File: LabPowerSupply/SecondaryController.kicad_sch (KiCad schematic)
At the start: 15 parts

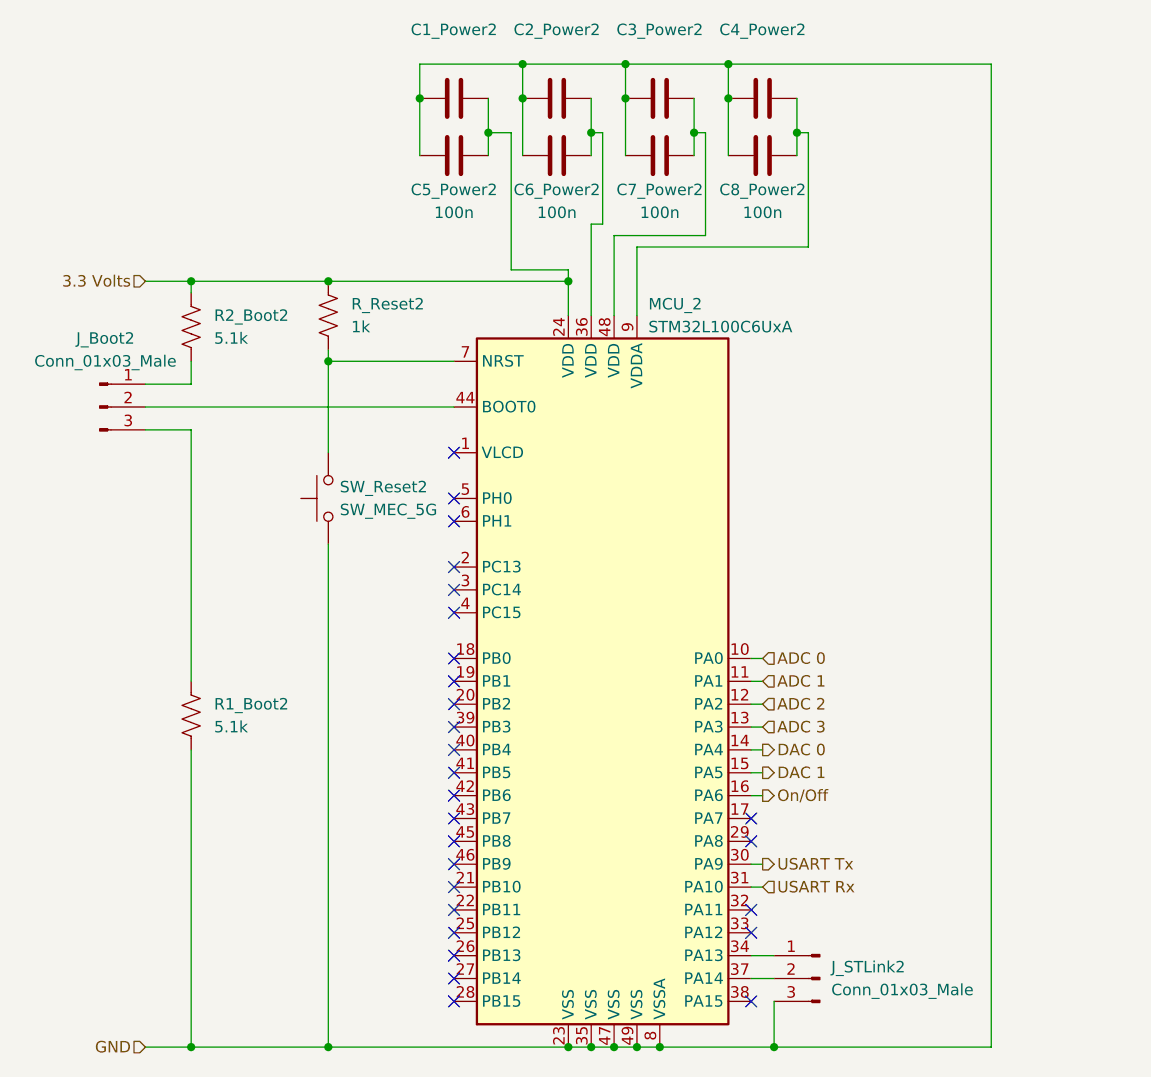
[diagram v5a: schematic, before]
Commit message: Added oscillator to mcu2
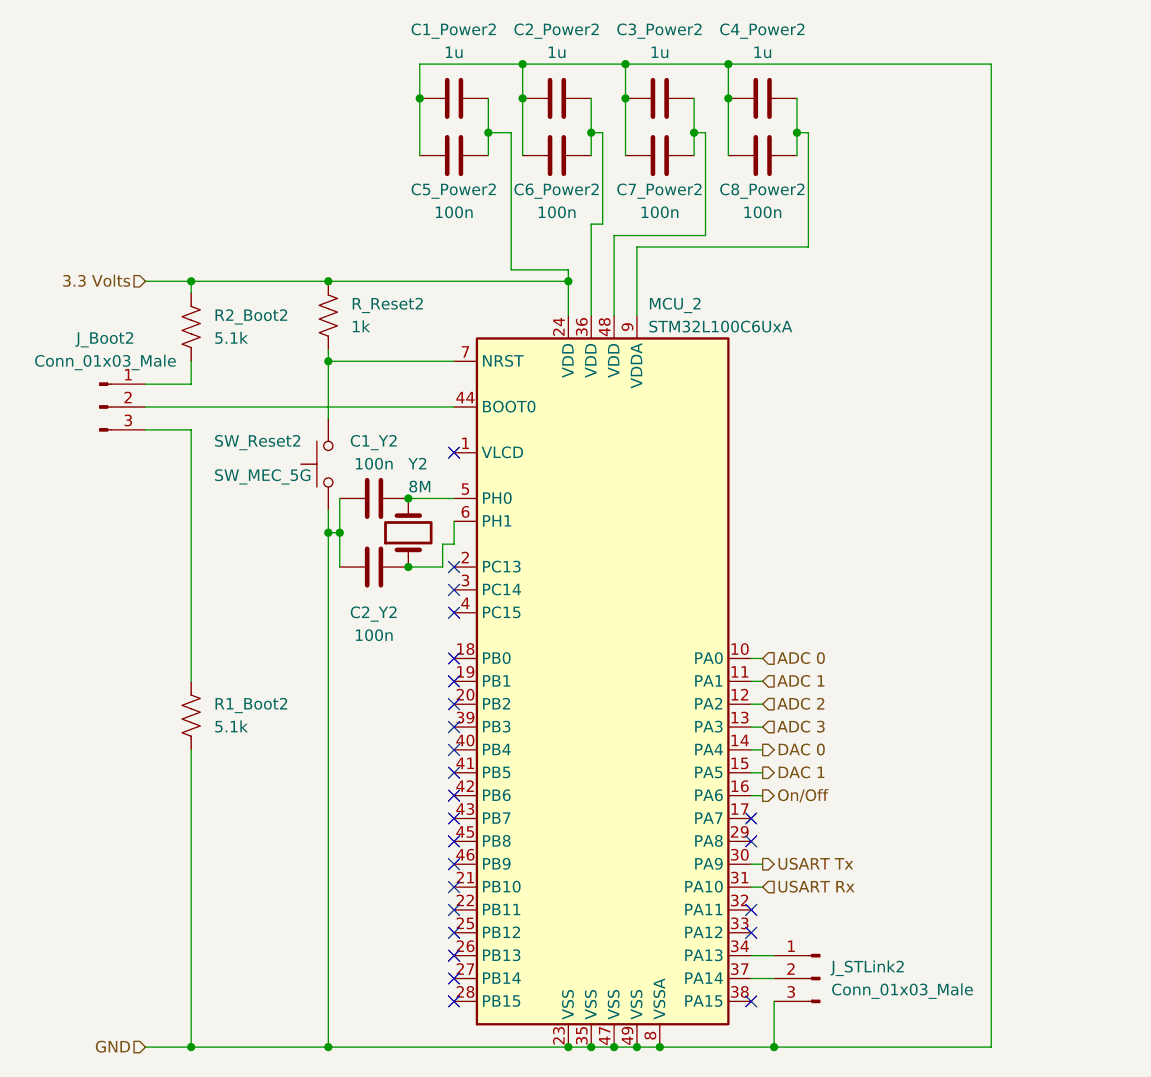
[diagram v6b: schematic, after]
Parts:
- added C1_Y2, C2_Y2: 100n, Capacitor_THT:C_Disc_D5.0mm_W2.5mm_P2.50mm, symbol Device:C
- added Y2: 8M, Crystal:Crystal_HC18-U_Vertical, symbol Device:Crystal
- C1_Power2, C2_Power2, C3_Power2, C4_Power2: value (none) -> 1u
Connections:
- net GND: now also C1_Y2.1, C2_Y2.1
- net at MCU_2.5 (PH0): now also C1_Y2.2, Y2.2
- net at MCU_2.6 (PH1): now also C2_Y2.2, Y2.1
- no-connect marks 27 -> 25
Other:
- moved on the sheet: SW_Reset2
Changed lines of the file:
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@@
   (junction (at 68.58 139.7) (diameter 0) (color 0 0 0 0)
   )
+  (junction (at 68.58 82.55) (diameter 0) (color 0 0 0 0)
+  )
   (junction (at 118.11 139.7) (diameter 0) (color 0 0 0 0)
   )
@@
   (junction (at 95.25 54.61) (diameter 0) (color 0 0 0 0)
   )
+  (junction (at 69.85 82.55) (diameter 0) (color 0 0 0 0)
+  )
+  (junction (at 77.47 86.36) (diameter 0) (color 0 0 0 0)
+  )
   (junction (at 90.17 34.29) (diameter 0) (color 0 0 0 0)
   )
@@
   )
   (junction (at 86.36 38.1) (diameter 0) (color 0 0 0 0)
+  )
+  (junction (at 77.47 78.74) (diameter 0) (color 0 0 0 0)
   )
   (junction (at 105.41 139.7) (diameter 0) (color 0 0 0 0)
@@
   (no_connect (at 82.55 88.9))
   (no_connect (at 82.55 91.44))
-  (no_connect (at 82.55 81.28))
   (no_connect (at 82.55 73.66))
-  (no_connect (at 82.55 78.74))
   (no_connect (at 82.55 96.52))
   (wire (pts (xy 90.17 34.29) (xy 90.17 40.64))
@@
     (stroke (width 0) (type default) (color 0 0 0 0))
   )
+  (wire (pts (xy 82.55 83.82) (xy 81.28 83.82))
+    (stroke (width 0) (type default) (color 0 0 0 0))
+  )
   (wire (pts (xy 88.9 53.34) (xy 95.25 53.34))
     (stroke (width 0) (type default) (color 0 0 0 0))
@@
     (stroke (width 0) (type default) (color 0 0 0 0))
   )
+  (wire (pts (xy 68.58 82.55) (xy 69.85 82.55))
+    (stroke (width 0) (type default) (color 0 0 0 0))
+  )
   (wire (pts (xy 95.25 53.34) (xy 95.25 54.61))
     (stroke (width 0) (type default) (color 0 0 0 0))
@@
     (stroke (width 0) (type default) (color 0 0 0 0))
   )
+  (wire (pts (xy 68.58 82.55) (xy 68.58 139.7))
+    (stroke (width 0) (type default) (color 0 0 0 0))
+  )
   (wire (pts (xy 86.36 34.29) (xy 86.36 38.1))
     (stroke (width 0) (type default) (color 0 0 0 0))
@@
     (stroke (width 0) (type default) (color 0 0 0 0))
   )
+  (wire (pts (xy 69.85 78.74) (xy 69.85 82.55))
+    (stroke (width 0) (type default) (color 0 0 0 0))
+  )
+  (wire (pts (xy 81.28 83.82) (xy 81.28 86.36))
+    (stroke (width 0) (type default) (color 0 0 0 0))
+  )
   (wire (pts (xy 142.24 139.7) (xy 118.11 139.7))
     (stroke (width 0) (type default) (color 0 0 0 0))
@@
     (stroke (width 0) (type default) (color 0 0 0 0))
   )
+  (wire (pts (xy 77.47 78.74) (xy 82.55 78.74))
+    (stroke (width 0) (type default) (color 0 0 0 0))
+  )
   (wire (pts (xy 97.79 38.1) (xy 97.79 40.64))
     (stroke (width 0) (type default) (color 0 0 0 0))
@@
     (stroke (width 0) (type default) (color 0 0 0 0))
   )
+  (wire (pts (xy 82.55 83.82) (xy 82.55 81.28))
+    (stroke (width 0) (type default) (color 0 0 0 0))
+  )
   (wire (pts (xy 68.58 54.61) (xy 95.25 54.61))
     (stroke (width 0) (type default) (color 0 0 0 0))
@@
     (stroke (width 0) (type default) (color 0 0 0 0))
   )
+  (wire (pts (xy 81.28 86.36) (xy 77.47 86.36))
+    (stroke (width 0) (type default) (color 0 0 0 0))
+  )
   (wire (pts (xy 142.24 30.48) (xy 113.03 30.48))
     (stroke (width 0) (type default) (color 0 0 0 0))
@@
     (stroke (width 0) (type default) (color 0 0 0 0))
   )
-  (wire (pts (xy 68.58 83.82) (xy 68.58 139.7))
+  (wire (pts (xy 69.85 82.55) (xy 69.85 86.36))
+    (stroke (width 0) (type default) (color 0 0 0 0))
+  )
+  (wire (pts (xy 68.58 80.01) (xy 68.58 82.55))
     (stroke (width 0) (type default) (color 0 0 0 0))
   )
@@
     (stroke (width 0) (type default) (color 0 0 0 0))
   )
-  (wire (pts (xy 68.58 63.5) (xy 68.58 73.66))
+  (wire (pts (xy 68.58 63.5) (xy 68.58 69.85))
     (stroke (width 0) (type default) (color 0 0 0 0))
   )
@@
     )
     (property "Datasheet" "~" (id 3) (at 116.84 40.64 0)
+      (effects (font (size 1.27 1.27)) hide)
+    )
+    (pin "1")
+    (pin "2")
+  )
+  (symbol (lib_id "Device:C") (at 73.66 86.36 90) (mirror x) (unit 1)
+    (in_bom yes) (on_board yes)
+    (property "Reference" "C2_Y2" (id 0) (at 73.66 91.44 90))
+    (property "Value" "100n" (id 1) (at 73.66 93.98 90))
+    (property "Footprint" "Capacitor_THT:C_Disc_D5.0mm_W2.5mm_P2.50mm" (id 2) (at 77.47 87.3252 0)
+      (effects (font (size 1.27 1.27)) hide)
+    )
+    (property "Datasheet" "~" (id 3) (at 73.66 86.36 0)
       (effects (font (size 1.27 1.27)) hide)
     )
@@
     (in_bom yes) (on_board yes) (fields_autoplaced)
     (property "Reference" "C1_Power2" (id 0) (at 82.55 26.67 90))
-    (property "Value" "" (id 1) (at 82.55 29.21 90))
+    (property "Value" "1u" (id 1) (at 82.55 29.21 90))
     (property "Footprint" "Capacitor_THT:C_Disc_D5.0mm_W2.5mm_P2.50mm" (id 2) (at 86.36 33.3248 0)
       (effects (font (size 1.27 1.27)) hide)
@@
     (in_bom yes) (on_board yes) (fields_autoplaced)
     (property "Reference" "C2_Power2" (id 0) (at 93.98 26.67 90))
-    (property "Value" "" (id 1) (at 93.98 29.21 90))
+    (property "Value" "1u" (id 1) (at 93.98 29.21 90))
     (property "Footprint" "Capacitor_THT:C_Disc_D5.0mm_W2.5mm_P2.50mm" (id 2) (at 97.79 33.3248 0)
       (effects (font (size 1.27 1.27)) hide)
@@
     (pin "2")
   )
+  (symbol (lib_id "Device:C") (at 73.66 78.74 90) (unit 1)
+    (in_bom yes) (on_board yes)
+    (property "Reference" "C1_Y2" (id 0) (at 73.66 72.39 90))
+    (property "Value" "100n" (id 1) (at 73.66 74.93 90))
+    (property "Footprint" "Capacitor_THT:C_Disc_D5.0mm_W2.5mm_P2.50mm" (id 2) (at 77.47 77.7748 0)
+      (effects (font (size 1.27 1.27)) hide)
+    )
+    (property "Datasheet" "~" (id 3) (at 73.66 78.74 0)
+      (effects (font (size 1.27 1.27)) hide)
+    )
+    (pin "1")
+    (pin "2")
+  )
   (symbol (lib_id "Device:C") (at 105.41 34.29 90) (unit 1)
     (in_bom yes) (on_board yes) (fields_autoplaced)
     (property "Reference" "C3_Power2" (id 0) (at 105.41 26.67 90))
-    (property "Value" "" (id 1) (at 105.41 29.21 90))
+    (property "Value" "1u" (id 1) (at 105.41 29.21 90))
     (property "Footprint" "Capacitor_THT:C_Disc_D5.0mm_W2.5mm_P2.50mm" (id 2) (at 109.22 33.3248 0)
       (effects (font (size 1.27 1.27)) hide)
@@
     (pin "2")
   )
+  (symbol (lib_id "Device:Crystal") (at 77.47 82.55 90) (unit 1)
+    (in_bom yes) (on_board yes)
+    (property "Reference" "Y2" (id 0) (at 77.47 74.93 90)
+      (effects (font (size 1.27 1.27)) (justify right))
+    )
+    (property "Value" "8M" (id 1) (at 77.47 77.47 90)
+      (effects (font (size 1.27 1.27)) (justify right))
+    )
+    (property "Footprint" "Crystal:Crystal_HC18-U_Vertical" (id 2) (at 77.47 82.55 0)
+      (effects (font (size 1.27 1.27)) hide)
+    )
+    (property "Datasheet" "~" (id 3) (at 77.47 82.55 0)
+      (effects (font (size 1.27 1.27)) hide)
+    )
+    (pin "1")
+    (pin "2")
+  )
   (symbol (lib_id "Device:C") (at 116.84 34.29 90) (unit 1)
     (in_bom yes) (on_board yes) (fields_autoplaced)
     (property "Reference" "C4_Power2" (id 0) (at 116.84 26.67 90))
-    (property "Value" "" (id 1) (at 116.84 29.21 90))
+    (property "Value" "1u" (id 1) (at 116.84 29.21 90))
     (property "Footprint" "Capacitor_THT:C_Disc_D5.0mm_W2.5mm_P2.50mm" (id 2) (at 120.65 33.3248 0)
       (effects (font (size 1.27 1.27)) hide)
@@
     (pin "2")
   )
-  (symbol (lib_id "Switch:SW_MEC_5G") (at 68.58 78.74 90) (unit 1)
-    (in_bom yes) (on_board yes) (fields_autoplaced)
-    (property "Reference" "SW_Reset2" (id 0) (at 69.85 77.4699 90)
+  (symbol (lib_id "Switch:SW_MEC_5G") (at 68.58 74.93 90) (unit 1)
+    (in_bom yes) (on_board yes)
+    (property "Reference" "SW_Reset2" (id 0) (at 55.88 72.39 90)
       (effects (font (size 1.27 1.27)) (justify right))
     )
-    (property "Value" "SW_MEC_5G" (id 1) (at 69.85 80.0099 90)
+    (property "Value" "SW_MEC_5G" (id 1) (at 55.88 76.2 90)
       (effects (font (size 1.27 1.27)) (justify right))
     )
-    (property "Footprint" "Button_Switch_SMD:SW_MEC_5GSH9" (id 2) (at 63.5 78.74 0)
-      (effects (font (size 1.27 1.27)) hide)
-    )
-    (property "Datasheet" "http://www.apem.com/int/index.php?controller=attachment&id_attachment=488" (id 3) (at 63.5 78.74 0)
-      (effects (font (size 1.27 1.27)) hide)
-    )
+    (property "Footprint" "Button_Switch_SMD:SW_MEC_5GSH9" (id 2) (at 63.5 74.93 0)
+      (effects (font (size 1.27 1.27)) hide)
+    )
+    (property "Datasheet" "http://www.apem.com/int/index.php?controller=attachment&id_attachment=488" (id 3) (at 63.5 74.93 0)
+      (effects (font (size 1.27 1.27)) hide)
+    )

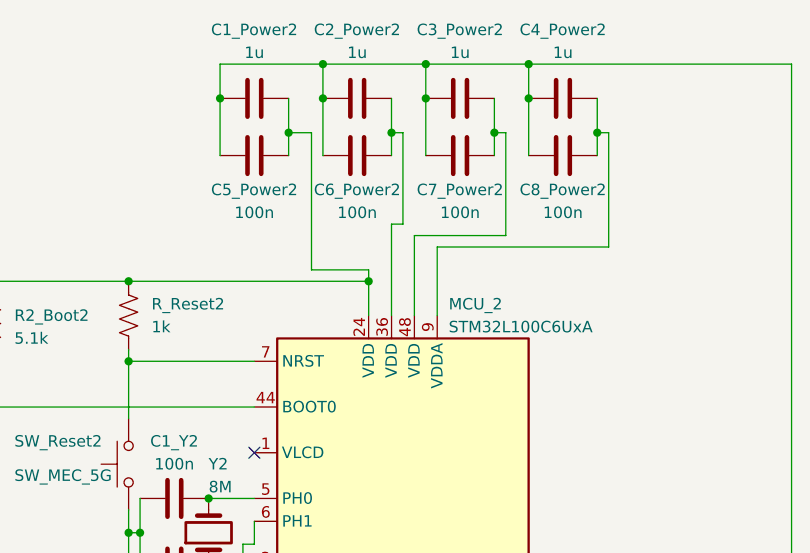
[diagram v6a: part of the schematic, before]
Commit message: Fixed mcu supply
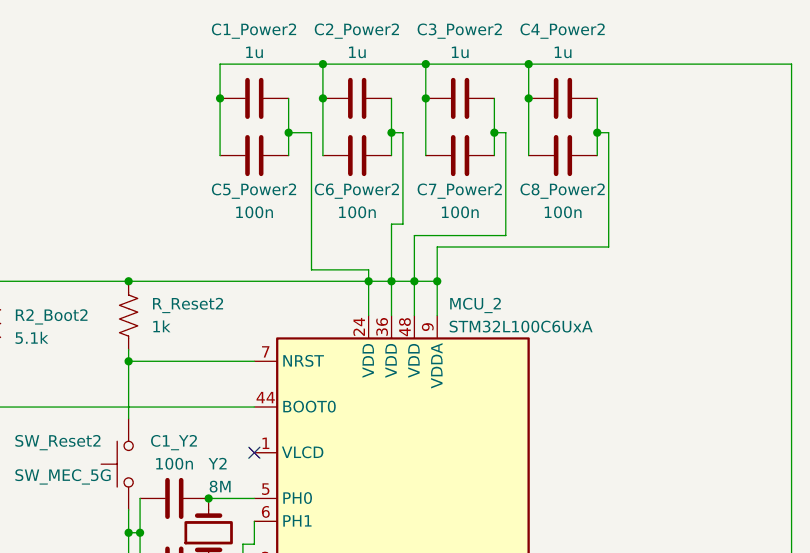
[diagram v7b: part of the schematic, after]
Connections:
- net 3.3 Volts: now also C2_Power2.2, C3_Power2.2, C4_Power2.2, C6_Power2.2, C7_Power2.2, C8_Power2.2, MCU_2.36 (VDD), MCU_2.48 (VDD), MCU_2.9 (VDDA)
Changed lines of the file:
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@@
   (junction (at 53.34 54.61) (diameter 0) (color 0 0 0 0)
   )
+  (junction (at 97.79 54.61) (diameter 0) (color 0 0 0 0)
+  )
   (junction (at 113.03 30.48) (diameter 0) (color 0 0 0 0)
   )
@@
   )
   (junction (at 77.47 86.36) (diameter 0) (color 0 0 0 0)
+  )
+  (junction (at 102.87 54.61) (diameter 0) (color 0 0 0 0)
+  )
+  (junction (at 100.33 54.61) (diameter 0) (color 0 0 0 0)
   )
   (junction (at 90.17 34.29) (diameter 0) (color 0 0 0 0)
@@
     (stroke (width 0) (type default) (color 0 0 0 0))
   )
+  (wire (pts (xy 100.33 54.61) (xy 102.87 54.61))
+    (stroke (width 0) (type default) (color 0 0 0 0))
+  )
   (wire (pts (xy 48.26 66.04) (xy 53.34 66.04))
     (stroke (width 0) (type default) (color 0 0 0 0))
   )
-  (wire (pts (xy 102.87 50.8) (xy 102.87 58.42))
+  (wire (pts (xy 102.87 50.8) (xy 102.87 54.61))
     (stroke (width 0) (type default) (color 0 0 0 0))
   )
@@
     (stroke (width 0) (type default) (color 0 0 0 0))
   )
+  (wire (pts (xy 95.25 54.61) (xy 97.79 54.61))
+    (stroke (width 0) (type default) (color 0 0 0 0))
+  )
   (wire (pts (xy 95.25 53.34) (xy 95.25 54.61))
     (stroke (width 0) (type default) (color 0 0 0 0))
@@
     (stroke (width 0) (type default) (color 0 0 0 0))
   )
+  (wire (pts (xy 97.79 54.61) (xy 100.33 54.61))
+    (stroke (width 0) (type default) (color 0 0 0 0))
+  )
   (wire (pts (xy 86.36 38.1) (xy 86.36 40.64))
     (stroke (width 0) (type default) (color 0 0 0 0))
@@
     (stroke (width 0) (type default) (color 0 0 0 0))
   )
+  (wire (pts (xy 97.79 54.61) (xy 97.79 58.42))
+    (stroke (width 0) (type default) (color 0 0 0 0))
+  )
   (wire (pts (xy 53.34 139.7) (xy 68.58 139.7))
     (stroke (width 0) (type default) (color 0 0 0 0))
@@
     (stroke (width 0) (type default) (color 0 0 0 0))
   )
+  (wire (pts (xy 102.87 54.61) (xy 102.87 58.42))
+    (stroke (width 0) (type default) (color 0 0 0 0))
+  )
   (wire (pts (xy 53.34 71.12) (xy 53.34 99.06))
     (stroke (width 0) (type default) (color 0 0 0 0))
@@
     (stroke (width 0) (type default) (color 0 0 0 0))
   )
-  (wire (pts (xy 100.33 49.53) (xy 100.33 58.42))
+  (wire (pts (xy 100.33 49.53) (xy 100.33 54.61))
     (stroke (width 0) (type default) (color 0 0 0 0))
   )
@@
     (stroke (width 0) (type default) (color 0 0 0 0))
   )
+  (wire (pts (xy 100.33 54.61) (xy 100.33 58.42))
+    (stroke (width 0) (type default) (color 0 0 0 0))
+  )
   (wire (pts (xy 68.58 139.7) (xy 95.25 139.7))
     (stroke (width 0) (type default) (color 0 0 0 0))
@@
     (stroke (width 0) (type default) (color 0 0 0 0))
   )
-  (wire (pts (xy 97.79 48.26) (xy 97.79 58.42))
-    (stroke (width 0) (type default) (color 0 0 0 0))
-  )
+  (wire (pts (xy 97.79 48.26) (xy 97.79 54.61))
+    (stroke (width 0) (type default) (color 0 0 0 0))
+  )

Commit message: another commit
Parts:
- C1_Power2, C2_Power2, C3_Power2, C4_Power2, C5_Power2, C6_Power2, C7_Power2, C8_Power2: footprint Capacitor_THT:C_Disc_D5.0mm_W2.5mm_P2.50mm -> Capacitor_SMD:C_0603_1608Metric
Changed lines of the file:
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@@
     (property "Reference" "C8_Power2" (id 0) (at 116.84 44.45 90))
     (property "Value" "100n" (id 1) (at 116.84 46.99 90))
-    (property "Footprint" "Capacitor_THT:C_Disc_D5.0mm_W2.5mm_P2.50mm" (id 2) (at 120.65 39.6748 0)
+    (property "Footprint" "Capacitor_SMD:C_0603_1608Metric" (id 2) (at 120.65 39.6748 0)
       (effects (font (size 1.27 1.27)) hide)
     )
@@
     (property "Reference" "C7_Power2" (id 0) (at 105.41 44.45 90))
     (property "Value" "100n" (id 1) (at 105.41 46.99 90))
-    (property "Footprint" "Capacitor_THT:C_Disc_D5.0mm_W2.5mm_P2.50mm" (id 2) (at 109.22 39.6748 0)
+    (property "Footprint" "Capacitor_SMD:C_0603_1608Metric" (id 2) (at 109.22 39.6748 0)
       (effects (font (size 1.27 1.27)) hide)
     )
@@
     (property "Reference" "C1_Power2" (id 0) (at 82.55 26.67 90))
     (property "Value" "1u" (id 1) (at 82.55 29.21 90))
-    (property "Footprint" "Capacitor_THT:C_Disc_D5.0mm_W2.5mm_P2.50mm" (id 2) (at 86.36 33.3248 0)
+    (property "Footprint" "Capacitor_SMD:C_0603_1608Metric" (id 2) (at 86.36 33.3248 0)
       (effects (font (size 1.27 1.27)) hide)
     )
@@
     (property "Reference" "C5_Power2" (id 0) (at 82.55 44.45 90))
     (property "Value" "100n" (id 1) (at 82.55 46.99 90))
-    (property "Footprint" "Capacitor_THT:C_Disc_D5.0mm_W2.5mm_P2.50mm" (id 2) (at 86.36 39.6748 0)
+    (property "Footprint" "Capacitor_SMD:C_0603_1608Metric" (id 2) (at 86.36 39.6748 0)
       (effects (font (size 1.27 1.27)) hide)
     )
@@
     (property "Reference" "C6_Power2" (id 0) (at 93.98 44.45 90))
     (property "Value" "100n" (id 1) (at 93.98 46.99 90))
-    (property "Footprint" "Capacitor_THT:C_Disc_D5.0mm_W2.5mm_P2.50mm" (id 2) (at 97.79 39.6748 0)
+    (property "Footprint" "Capacitor_SMD:C_0603_1608Metric" (id 2) (at 97.79 39.6748 0)
       (effects (font (size 1.27 1.27)) hide)
     )
@@
     (property "Reference" "C2_Power2" (id 0) (at 93.98 26.67 90))
     (property "Value" "1u" (id 1) (at 93.98 29.21 90))
-    (property "Footprint" "Capacitor_THT:C_Disc_D5.0mm_W2.5mm_P2.50mm" (id 2) (at 97.79 33.3248 0)
+    (property "Footprint" "Capacitor_SMD:C_0603_1608Metric" (id 2) (at 97.79 33.3248 0)
       (effects (font (size 1.27 1.27)) hide)
     )
@@
     (property "Reference" "C3_Power2" (id 0) (at 105.41 26.67 90))
     (property "Value" "1u" (id 1) (at 105.41 29.21 90))
-    (property "Footprint" "Capacitor_THT:C_Disc_D5.0mm_W2.5mm_P2.50mm" (id 2) (at 109.22 33.3248 0)
+    (property "Footprint" "Capacitor_SMD:C_0603_1608Metric" (id 2) (at 109.22 33.3248 0)
       (effects (font (size 1.27 1.27)) hide)
     )
@@
     (property "Reference" "C4_Power2" (id 0) (at 116.84 26.67 90))
     (property "Value" "1u" (id 1) (at 116.84 29.21 90))
-    (property "Footprint" "Capacitor_THT:C_Disc_D5.0mm_W2.5mm_P2.50mm" (id 2) (at 120.65 33.3248 0)
-      (effects (font (size 1.27 1.27)) hide)
-    )
+    (property "Footprint" "Capacitor_SMD:C_0603_1608Metric" (id 2) (at 120.65 33.3248 0)
+      (effects (font (size 1.27 1.27)) hide)
+    )
